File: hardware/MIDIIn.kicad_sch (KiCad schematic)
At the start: 6 parts, among them J301 SJ2-25404B-SMT-TR, U301 TLP2361

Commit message: Refresh
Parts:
- D301: Manufacturer (none) -> ROHM Semiconductor; Mouser (none) -> 755-RB501SM-30FHT2R; Product (none) -> RB501SM-30FHT2R
- J301: Manufacturer (none) -> Same Sky; Mouser (none) -> 490-SJ2-25404BSMT-TR; Product (none) -> SJ2-25404B-SMT-TR
- U301: Manufacturer (none) -> Toshiba; Mouser (none) -> 757-TLP2361TPRE; Product (none) -> TLP2361(TPR,E

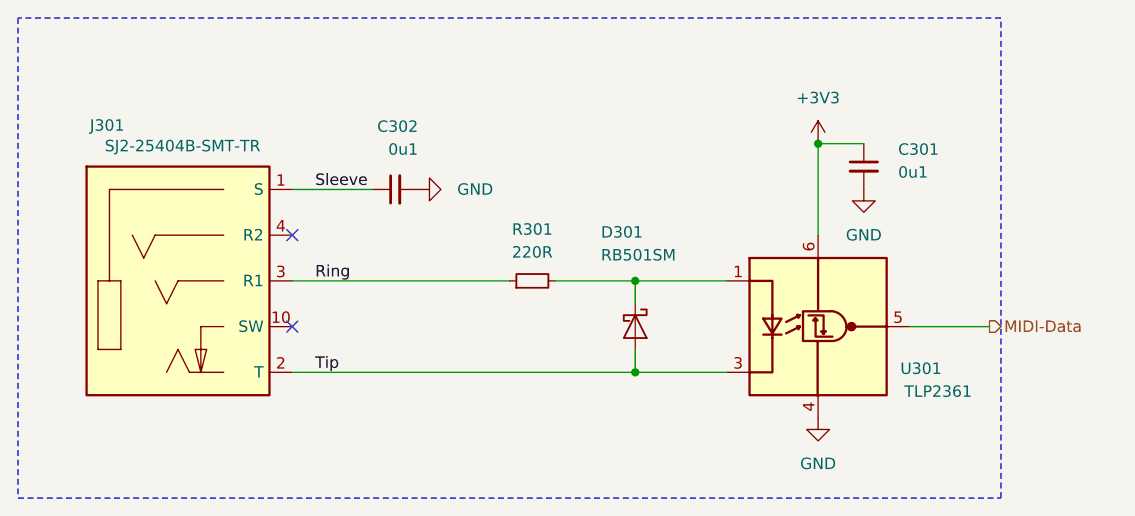
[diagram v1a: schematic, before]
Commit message: Replace Order_Number
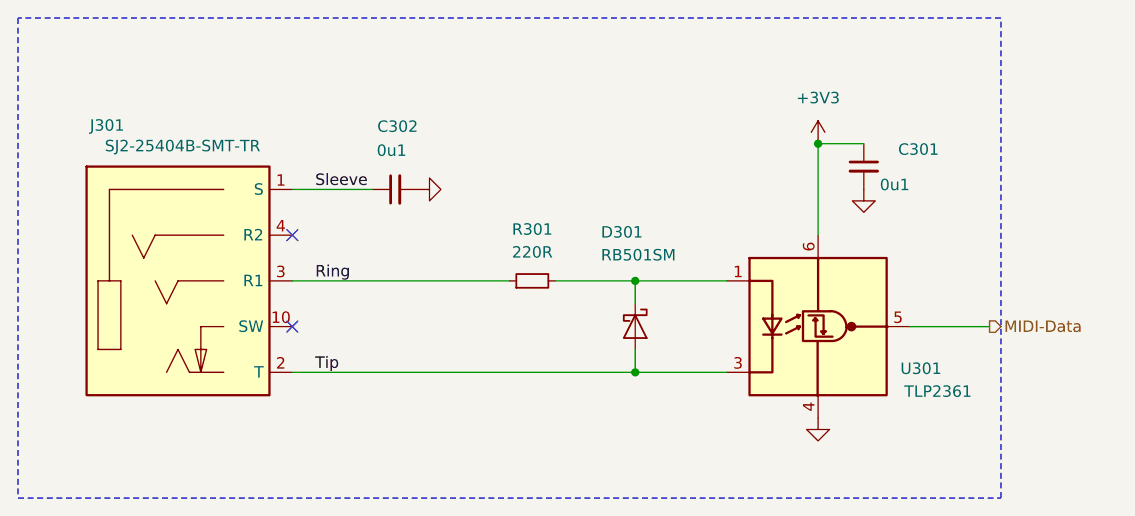
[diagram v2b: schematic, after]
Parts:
- C301, C302: footprint Capacitor_SMD:C_0603_1608Metric -> V2_Capacitor_SMD:C_0603; symbol Device:C_Small -> V2_Device:C_0603_0u1; Manufacturer (none) -> TDK; Mouser (none) -> 810-CGA3E2X7R1H104MA; Product (none) -> CGA3E2X7R1H104M080AA; Rating (none) -> 50V
- D301: footprint Diode_SMD:D_SOD-523 -> V2_Diode_SMD:D_SOD-523
- R301: footprint Resistor_SMD:R_0603_1608Metric -> V2_Resistor_SMD:R_0603; symbol Device:R_Small -> V2_Device:R_0603_220R; Manufacturer (none) -> Vishay; Mouser (none) -> 71-CRCW0603220RFKEAH; Product (none) -> CRCW0603220RFKEAHP; Rating (none) -> 330mW
- U301: footprint Package_SO:SO-5-6_4.55x3.7mm_P1.27mm -> V2_Package_SO:SO-5-6_4.55x3.7mm_P1.27mm

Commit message: Update Library
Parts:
- C301, C302: symbol V2_Device:C_0603_0u1 -> V2_Capacitor:0603_0u1
- R301: symbol V2_Device:R_0603_220R -> V2_Resistor:0603_220R

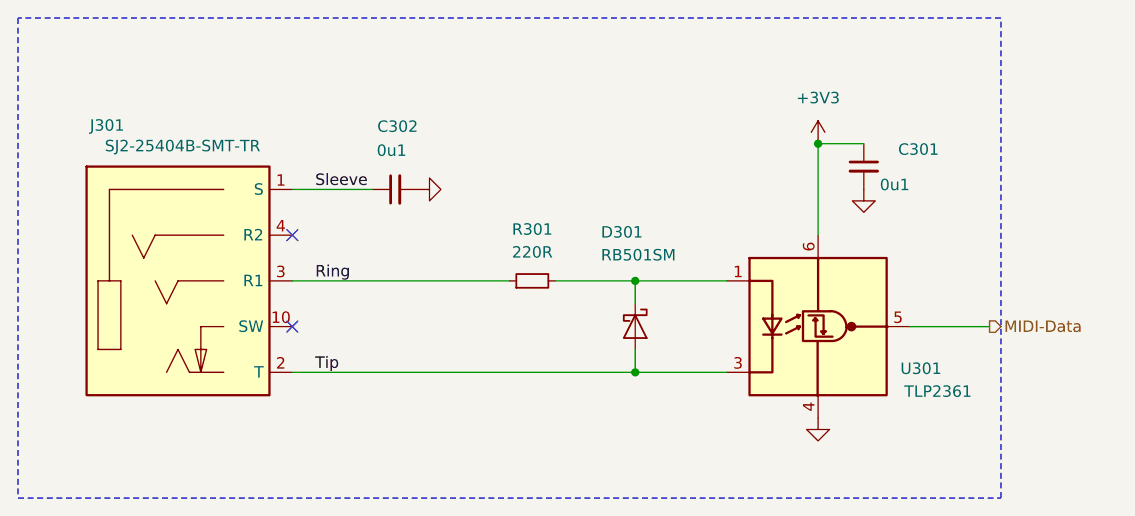
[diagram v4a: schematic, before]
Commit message: Replace diode
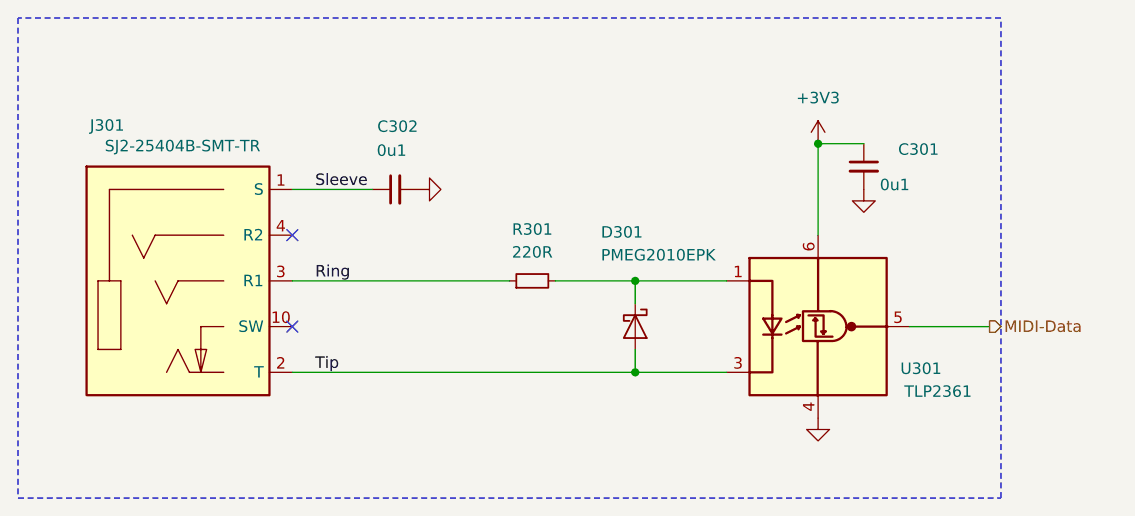
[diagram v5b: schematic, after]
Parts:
- D301: value RB501SM -> PMEG2010EPK; footprint V2_Diode_SMD:D_SOD-523 -> V2_Diode_SMD:D_SOD-1608; symbol V2_Diode:RB501SM -> V2_Diode:PMEG2010EPK; Manufacturer ROHM Semiconductor -> Nexperia; Mouser 755-RB501SM-30FHT2R -> 771-PMEG2010EPK; Product RB501SM-30FHT2R -> PMEG2010EPK; Rating (none) -> 20V
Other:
- title: MIDI In -> V2 radio
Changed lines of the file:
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@@
 (kicad_sch
-	(version 20250114)
+	(version 20260306)
 	(generator "eeschema")
-	(generator_version "9.0")
+	(generator_version "10.0")
 	(paper "A4")
 	(title_block
-		(title "MIDI In")
-		(date "2025-09-19")
-		(rev "3")
+		(title "V2 radio")
+		(date "2026-03-30")
+		(rev "2026-03-30")
 	)

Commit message: Update
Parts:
- C301: renamed from C302; Id (none) -> Capacitor:${SYMBOL_NAME}
- C302: renamed from C301; Id (none) -> Capacitor:${SYMBOL_NAME}
- D301: Id (none) -> Diode:${SYMBOL_NAME}
- J301: Id (none) -> Audio:${SYMBOL_NAME}; Rating (none) -> 2.5mm
- R301: Id (none) -> Resistor:${SYMBOL_NAME}
- U301: Id (none) -> Optocoupler:${SYMBOL_NAME}; Rating (none) -> 15Mbps
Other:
- company: (none) -> Versio Duo
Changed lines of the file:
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@@
 	(title_block
 		(title "V2 radio")
-		(date "2026-03-30")
-		(rev "2026-03-30")
+		(date "2026-04-14")
+		(rev "2026-04-14")
+		(company "Versio Duo")
+		(comment 1 "433 MHz MIDI bridge")
 	)

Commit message: Good Bye Imperial
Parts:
- C301, C302: footprint V2_Capacitor_SMD:C_0603 -> V2_Capacitor_SMD:C_1608; symbol V2_Capacitor:0603_0u1 -> V2_Capacitor:1608_0u1
- R301: footprint V2_Resistor_SMD:R_0603 -> V2_Resistor_SMD:R_1608; symbol V2_Resistor:0603_220R -> V2_Resistor:1608_220R
